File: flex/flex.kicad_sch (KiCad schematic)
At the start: 86 parts, among them J1 NA_Conn_01x04_Female, J2 NA_Conn_01x05_Female, J3 NA_Conn_01x03_Female, J4 NA_Conn_01x06_Female, J5 NA_Conn_01x03_Female, SW10 NA_SW_Push, SW11 NA_SW_Push, SW12 NA_SW_Push, SW15 NA_SW_Push, SW16 NA_SW_Push, SW17 NA_SW_Push, SW20 NA_SW_Push, SW21 NA_SW_Push, SW22 NA_SW_Push, SW24 NA_SW_Push, SW25 NA_SW_Push, SW26 NA_SW_Push, SW6 NA_SW_Push, SW7 NA_SW_Push, SW8 NA_SW_Push

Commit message: work
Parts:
- added Mousebite1, Mousebite10, Mousebite11, Mousebite12, Mousebite2, Mousebite3, Mousebite4, Mousebite5, Mousebite6, Mousebite7, Mousebite8, Mousebite9: ~, customs:mousebite, symbol customs:mousebite

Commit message: add LED in/out/vcc/gnd connectors
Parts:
- added J100, J101, J102, J103, J104, J105, J106, J92, J93, J94, J95, J96, J97, J98, J99: Conn_01x01_Socket, custom:PinHeader_1x01_P1.27mm_Vertical_VCC, symbol Connector:Conn_01x01_Socket
- added J107, J108, J109, J110, J111, J112, J113, J114, J115, J116, J117, J118, J119, J120, J121: Conn_01x01_Socket, custom:PinHeader_1x01_P1.27mm_Vertical_GND, symbol Connector:Conn_01x01_Socket
- added J61, J63, J65, J67, J69, J71, J73, J75, J77, J79, J82, J84, J86, J88, J90: Conn_01x01_Socket, custom:PinHeader_1x01_P1.27mm_Vertical_IN, symbol Connector:Conn_01x01_Socket
- added J62, J64, J66, J68, J70, J72, J74, J76, J78, J81, J83, J85, J87, J89, J91: Conn_01x01_Socket, custom:PinHeader_1x01_P1.27mm_Vertical_OUT, symbol Connector:Conn_01x01_Socket
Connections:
- net Dout: now also J91.1 (Pin_1)
- net Gnd: now also J107.1 (Pin_1), J108.1 (Pin_1), J109.1 (Pin_1), J110.1 (Pin_1), J111.1 (Pin_1), J112.1 (Pin_1), J113.1 (Pin_1), J114.1 (Pin_1), J115.1 (Pin_1), J116.1 (Pin_1), J117.1 (Pin_1), J118.1 (Pin_1), J119.1 (Pin_1), J120.1 (Pin_1), J121.1 (Pin_1)
- net Vcc: now also J100.1 (Pin_1), J101.1 (Pin_1), J102.1 (Pin_1), J103.1 (Pin_1), J104.1 (Pin_1), J105.1 (Pin_1), J106.1 (Pin_1), J92.1 (Pin_1), J93.1 (Pin_1), J94.1 (Pin_1), J95.1 (Pin_1), J96.1 (Pin_1), J97.1 (Pin_1), J98.1 (Pin_1), J99.1 (Pin_1)
- net at D39.1 (DOUT), D40.1 (DOUT), D41.3 (DIN)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: now also J76.1 (Pin_1), J77.1 (Pin_1)
- net at D37.1 (DOUT), D38.1 (DOUT), D39.3 (DIN)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: now also J74.1 (Pin_1), J75.1 (Pin_1)
- net at D23.1 (DOUT), D24.1 (DOUT), D25.3 (DIN)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: now also J70.1 (Pin_1), J71.1 (Pin_1)
- net at D21.1 (DOUT), D22.1 (DOUT), D23.3 (DIN)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: now also J68.1 (Pin_1), J69.1 (Pin_1)
- net at D21.3 (DIN), D22.3 (DIN), D33.1 (DOUT)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: now also J66.1 (Pin_1), J67.1 (Pin_1)
- net at D33.3 (DIN), D34.3 (DIN), D7.1 (DOUT)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: now also J64.1 (Pin_1), J65.1 (Pin_1)
- net at D25.1 (DOUT), D26.1 (DOUT), D37.3 (DIN)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: now also J72.1 (Pin_1), J73.1 (Pin_1)
- net at D47.1 (DOUT), D48.1 (DOUT), D49.3 (DIN)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: now also J81.1 (Pin_1), J82.1 (Pin_1)
- net at D41.1 (DOUT), D42.1 (DOUT), D47.3 (DIN)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: now also J78.1 (Pin_1), J79.1 (Pin_1)
- net at D57.1 (DOUT), D58.1 (DOUT), D59.3 (DIN)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: now also J89.1 (Pin_1)
- net at D55.1 (DOUT), D56.1 (DOUT), D57.3 (DIN)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: now also J87.1 (Pin_1), J88.1 (Pin_1)
- net at D5.1 (DOUT), D6.1 (DOUT), D7.3 (DIN)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: now also J62.1 (Pin_1), J63.1 (Pin_1)
- net at D5.3 (DIN), D6.3 (DIN), R1.2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: now also J61.1 (Pin_1)
- net at D49.1 (DOUT), D50.1 (DOUT), D51.3 (DIN)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: now also J83.1 (Pin_1), J84.1 (Pin_1)

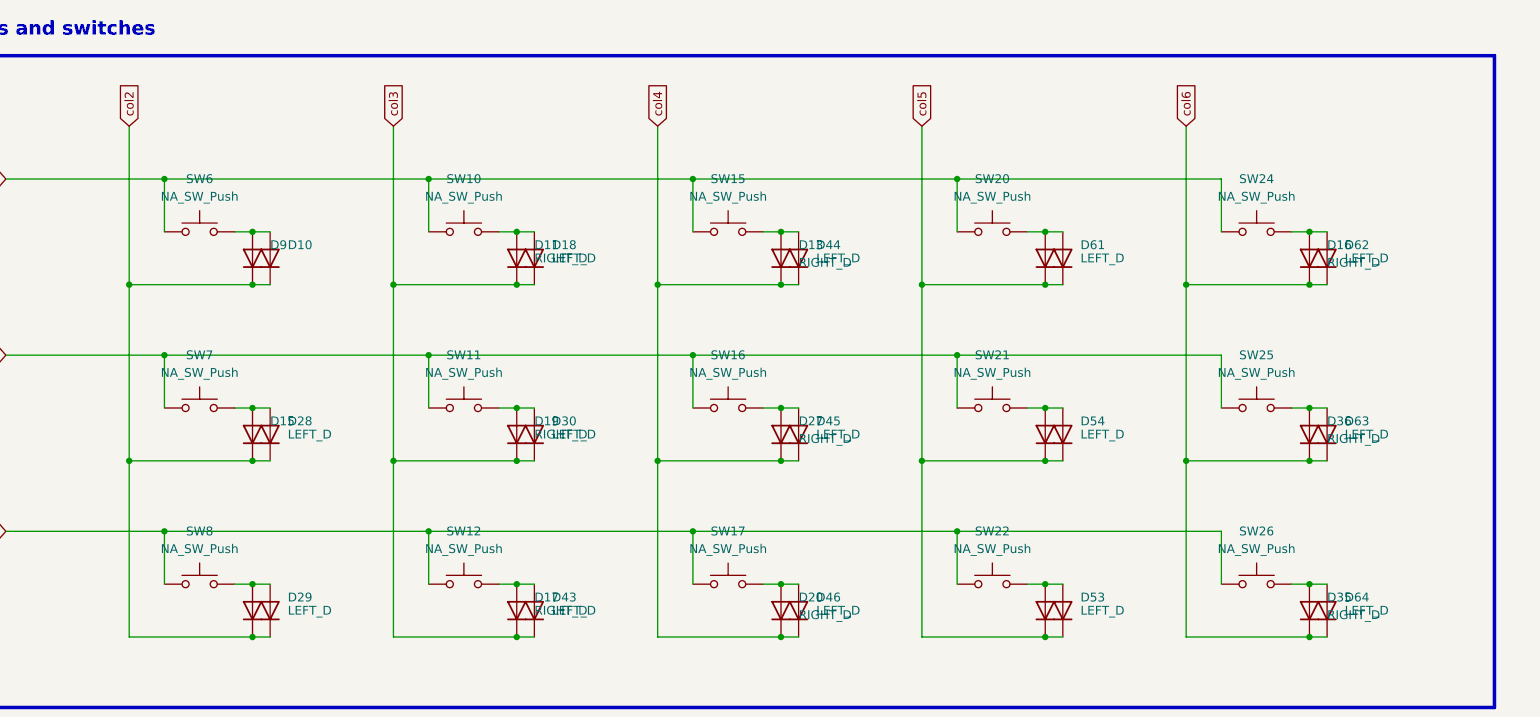
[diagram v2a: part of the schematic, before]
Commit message: place breakouts
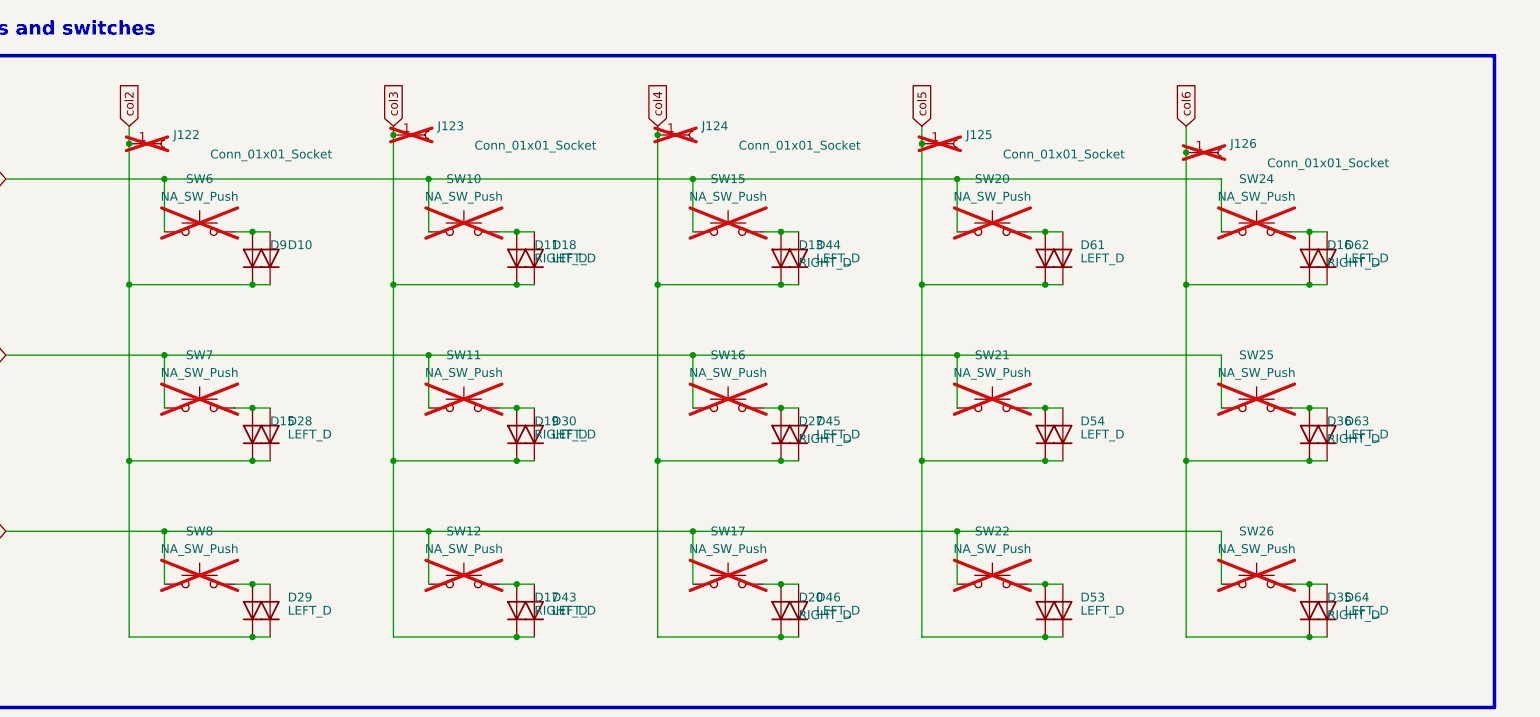
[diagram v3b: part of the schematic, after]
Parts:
- added J122, J123, J124, J125, J126: Conn_01x01_Socket, custom:PinHeader_1x01_P1.27mm_Vertical, symbol Connector:Conn_01x01_Socket
- J100, J101, J102, J103, J104, J105, J106, J107, J108, J109, J110, J111, J112, J113, J114, J115, J116, J117, J118, J119, J120, J121, J61, J62, J63, J64, J65, J66, J67, J68, J69, J70, J71, J72, J73, J74, J75, J76, J77, J78, J79, J81, J82, J83, J84, J85, J86, J87, J88, J89, J90, J91, J92, J93, J94, J95, J96, J97, J98, J99, Mousebite1, Mousebite10, Mousebite11, Mousebite12, Mousebite2, Mousebite3, Mousebite4, Mousebite5, Mousebite6, Mousebite7, Mousebite8, Mousebite9: now left out of the parts list
- SW10, SW11, SW12, SW15, SW16, SW17, SW20, SW21, SW22, SW24, SW25, SW26, SW6, SW7, SW8: now not fitted; now left out of the parts list
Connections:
- net col2: now also J122.1 (Pin_1)
- net col3: now also J123.1 (Pin_1)
- net col4: now also J124.1 (Pin_1)
- net col5: now also J125.1 (Pin_1)
- net col6: now also J126.1 (Pin_1)
